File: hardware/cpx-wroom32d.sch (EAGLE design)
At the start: 39 parts, among them Q1 mmbt2222, Q2 mmbt2222, U1 ESP32-WROOM-32D

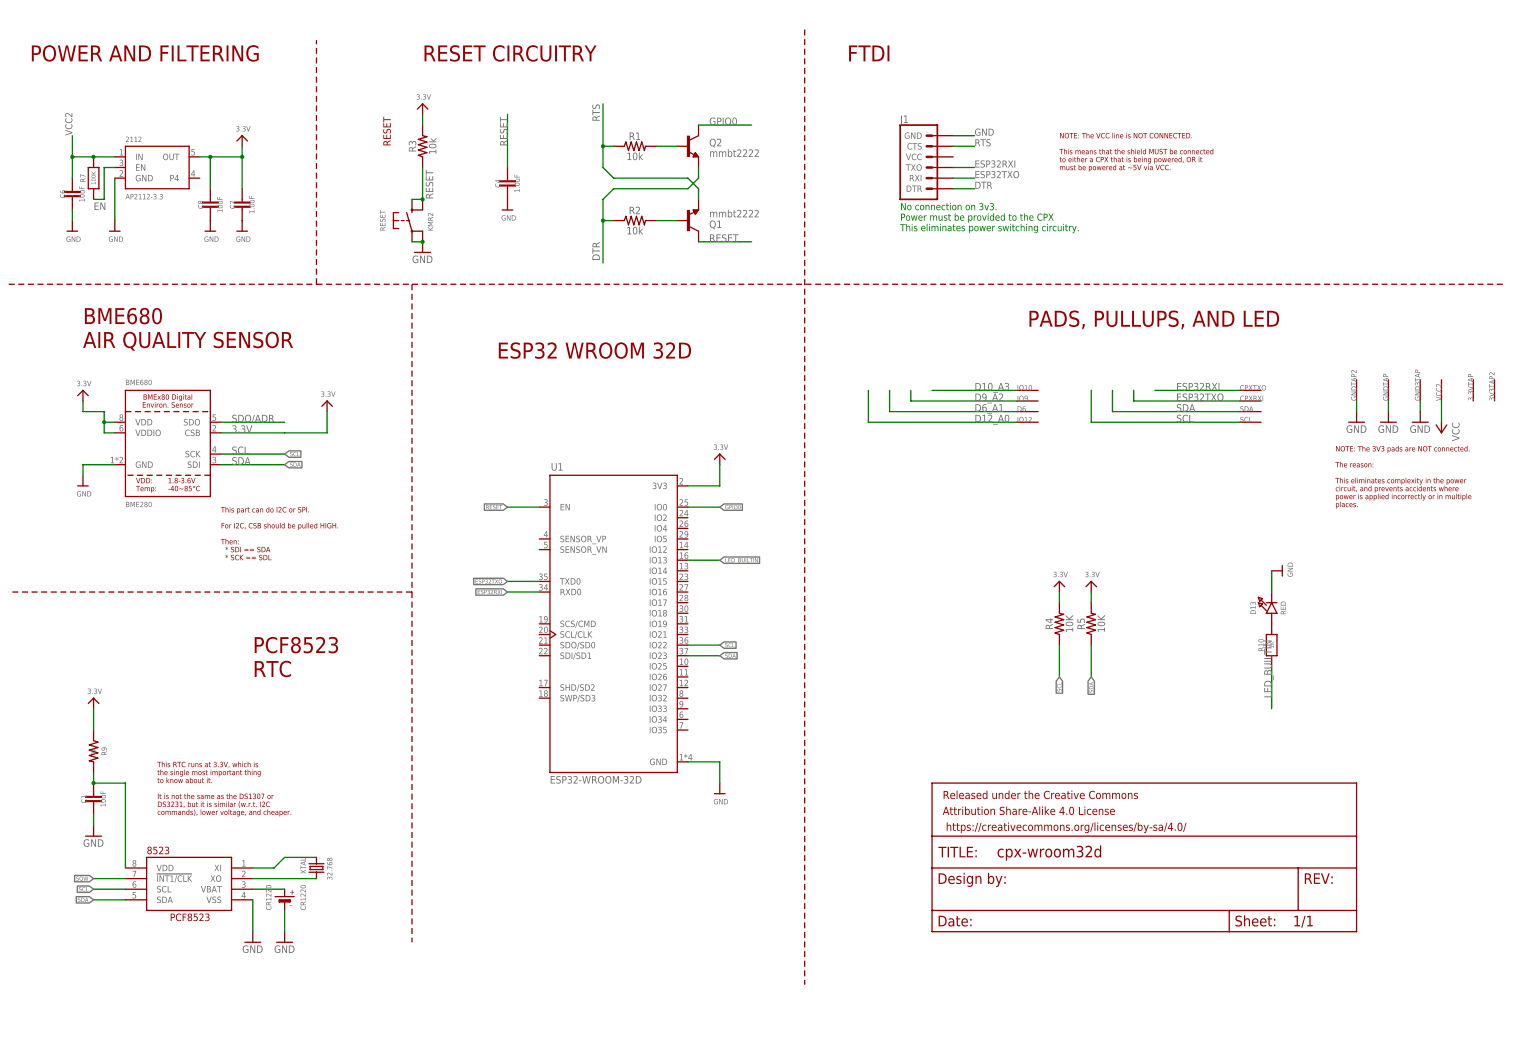
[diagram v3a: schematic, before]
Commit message: Cleaned up labeling, schematic.
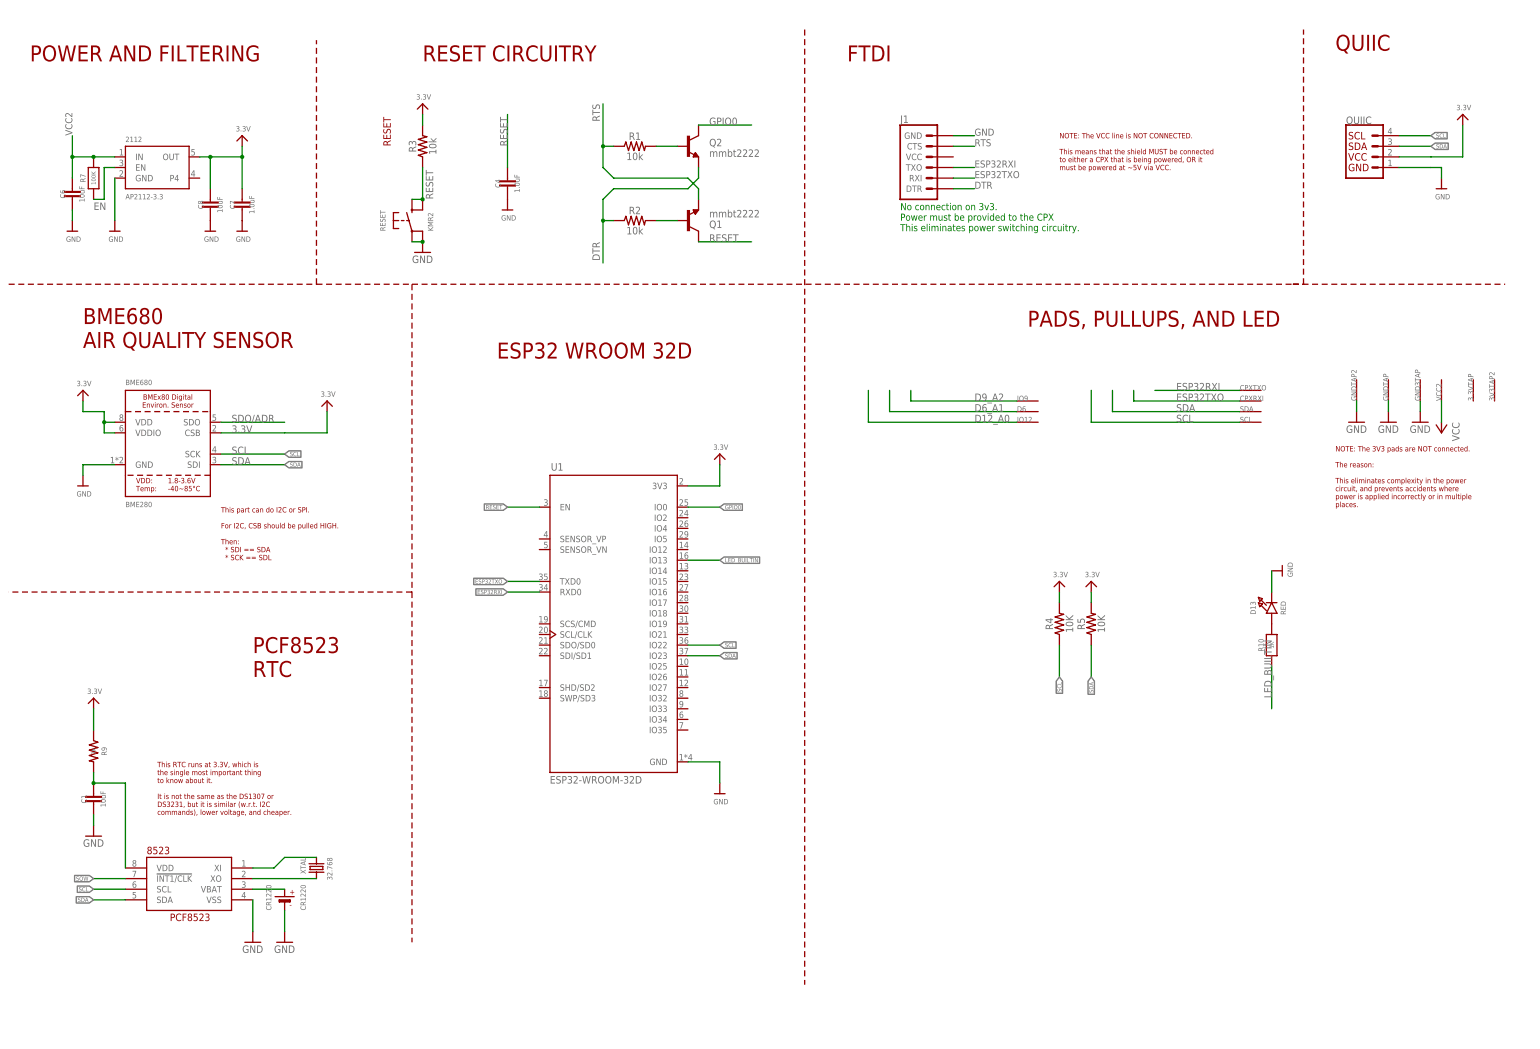
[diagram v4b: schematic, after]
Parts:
- removed FRAME1: FRAME-LETTERNO_PACKAGE, SparkFun-Aesthetics:FRAME-LETTERNO_PACKAGE
- removed IO10: SEWTAP-ALLIGATOR, microbuilder:SEWTAP-ALLIGATOR
- added QUIIC: (no value), SparkFun-Connectors:QWIIC_CONNECTORJS-1MM
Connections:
- removed net D10_A3: IO10.SEW
- net 3.3V: now also QUIIC.VCC
- net GND: now also QUIIC.GND
- net SCL: now also QUIIC.SCL
- net SDA: now also QUIIC.SDA
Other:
- note added: "QUIIC"
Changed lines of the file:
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@@
 <part name="SDA" library="microbuilder" deviceset="SEWTAP" device="-ALLIGATOR"/>
 <part name="P+2" library="supply1" deviceset="VCC" device=""/>
-<part name="IO10" library="microbuilder" deviceset="SEWTAP" device="-ALLIGATOR"/>
 <part name="IO9" library="microbuilder" deviceset="SEWTAP" device="-ALLIGATOR"/>
 <part name="D6" library="microbuilder" deviceset="SEWTAP" device="-ALLIGATOR"/>
@@
 <part name="U$12" library="microbuilder" deviceset="3.3V" device=""/>
 <part name="U$9" library="microbuilder" deviceset="3.3V" device=""/>
-<part name="FRAME1" library="SparkFun-Aesthetics" library_urn="urn:adsk.eagle:library:507" deviceset="FRAME-LETTER" device="NO_PACKAGE" package3d_urn="urn:adsk.eagle:package:37104/1"/>
+<part name="QUIIC" library="SparkFun-Connectors" library_urn="urn:adsk.eagle:library:513" deviceset="QWIIC_CONNECTOR" device="JS-1MM" package3d_urn="urn:adsk.eagle:package:38096/1"/>
+<part name="U$11" library="microbuilder" deviceset="3.3V" device=""/>
+<part name="U$14" library="microbuilder" deviceset="GND" device=""/>
 </parts>
 <sheets>
@@
 <wire x1="12.7" y1="187.96" x2="86.36" y2="187.96" width="0.1524" layer="94" style="shortdash"/>
 <wire x1="86.36" y1="187.96" x2="109.22" y2="187.96" width="0.1524" layer="94" style="shortdash"/>
-<wire x1="109.22" y1="187.96" x2="370.84" y2="187.96" width="0.1524" layer="94" style="shortdash"/>
+<wire x1="109.22" y1="187.96" x2="320.04" y2="187.96" width="0.1524" layer="94" style="shortdash"/>
+<wire x1="320.04" y1="187.96" x2="370.84" y2="187.96" width="0.1524" layer="94" style="shortdash"/>
 <wire x1="203.2" y1="248.92" x2="203.2" y2="20.32" width="0.1524" layer="94" style="shortdash"/>
 <wire x1="109.22" y1="187.96" x2="109.22" y2="114.3" width="0.1524" layer="94" style="shortdash"/>
@@
 power is applied incorrectly or in multiple
 places.</text>
+<wire x1="320.04" y1="187.96" x2="322.58" y2="187.96" width="0.1524" layer="94" style="shortdash"/>
+<wire x1="322.58" y1="187.96" x2="322.58" y2="248.92" width="0.1524" layer="94" style="shortdash"/>
+<text x="330.2" y="243.84" size="3.81" layer="94" font="vector" ratio="12">QUIIC</text>
 </plain>
 <instances>
@@
 <attribute name="VALUE" x="358.14" y="154.94" size="1.778" layer="96" rot="R270"/>
 </instance>
-<instance part="IO10" gate="G$1" x="254" y="162.56" smashed="yes">
-<attribute name="NAME" x="254" y="162.56" size="1.27" layer="95" font="vector"/>
-</instance>
 <instance part="IO9" gate="G$1" x="254" y="160.02" smashed="yes">
 <attribute name="NAME" x="254" y="160.02" size="1.27" layer="95" font="vector"/>
@@
 <attribute name="VALUE" x="87.376" y="161.036" size="1.27" layer="96"/>
 </instance>
-<instance part="FRAME1" gate="V" x="233.68" y="33.02" smashed="yes">
-<attribute name="LAST_DATE_TIME" x="246.38" y="34.29" size="2.54" layer="94" font="vector"/>
-<attribute name="SHEET" x="320.04" y="34.29" size="2.54" layer="94" font="vector"/>
-<attribute name="DRAWING_NAME" x="249.174" y="50.8" size="2.7432" layer="94" font="vector"/>
+<instance part="QUIIC" gate="J1" x="337.82" y="218.44" smashed="yes">
+<attribute name="VALUE" x="332.74" y="213.106" size="1.778" layer="96" font="vector" align="top-left"/>
+<attribute name="NAME" x="332.74" y="226.314" size="1.778" layer="95" font="vector"/>
+</instance>
+<instance part="U$11" gate="G$1" x="360.68" y="228.6" smashed="yes">
+<attribute name="VALUE" x="359.156" y="229.616" size="1.27" layer="96"/>
+</instance>
+<instance part="U$14" gate="G$1" x="355.6" y="210.82" smashed="yes">
+<attribute name="VALUE" x="354.076" y="208.28" size="1.27" layer="96"/>
 </instance>
 </instances>
@@
 <pinref part="U$4" gate="G$1" pin="GND"/>
 <pinref part="BME680" gate="G$1" pin="GND"/>
+</segment>
+<segment>
+<pinref part="QUIIC" gate="J1" pin="GND"/>
+<wire x1="345.44" y1="215.9" x2="353.06" y2="215.9" width="0.1524" layer="91"/>
+<pinref part="U$14" gate="G$1" pin="GND"/>
+<wire x1="353.06" y1="215.9" x2="355.6" y2="215.9" width="0.1524" layer="91"/>
+<wire x1="355.6" y1="215.9" x2="355.6" y2="213.36" width="0.1524" layer="91"/>
 </segment>
 </net>
@@
 <pinref part="U$9" gate="G$1" pin="3.3V"/>
 </segment>
+<segment>
+<pinref part="QUIIC" gate="J1" pin="VCC"/>
+<wire x1="345.44" y1="218.44" x2="353.06" y2="218.44" width="0.1524" layer="91"/>
+<wire x1="353.06" y1="218.44" x2="360.68" y2="218.44" width="0.1524" layer="91"/>
+<wire x1="360.68" y1="218.44" x2="360.68" y2="226.06" width="0.1524" layer="91"/>
+<pinref part="U$11" gate="G$1" pin="3.3V"/>
+</segment>
 </net>
 <net name="D12_A0" class="0">
@@
 <label x="78.74" y="147.32" size="1.016" layer="95" xref="yes"/>
 </segment>
+<segment>
+<pinref part="QUIIC" gate="J1" pin="SCL"/>
+<wire x1="345.44" y1="223.52" x2="353.06" y2="223.52" width="0.1524" layer="91"/>
+<label x="353.06" y="223.52" size="1.016" layer="95" xref="yes"/>
+</segment>
 </net>
 <net name="SDA" class="0">
@@
 <label x="78.74" y="144.78" size="1.016" layer="95" xref="yes"/>
 </segment>
+<segment>
+<pinref part="QUIIC" gate="J1" pin="SDA"/>
+<wire x1="345.44" y1="220.98" x2="353.06" y2="220.98" width="0.1524" layer="91"/>
+<label x="353.06" y="220.98" size="1.016" layer="95" xref="yes"/>
+</segment>
 </net>
 <net name="ESP32TXO" class="0">
@@
 </segment>
 </net>
-<net name="D10_A3" class="0">
-<segment>
-<wire x1="233.68" y1="162.56" x2="254" y2="162.56" width="0.1524" layer="91"/>
-<label x="243.84" y="162.56" size="1.778" layer="95"/>
-<pinref part="IO10" gate="G$1" pin="SEW"/>
-</segment>
-</net>

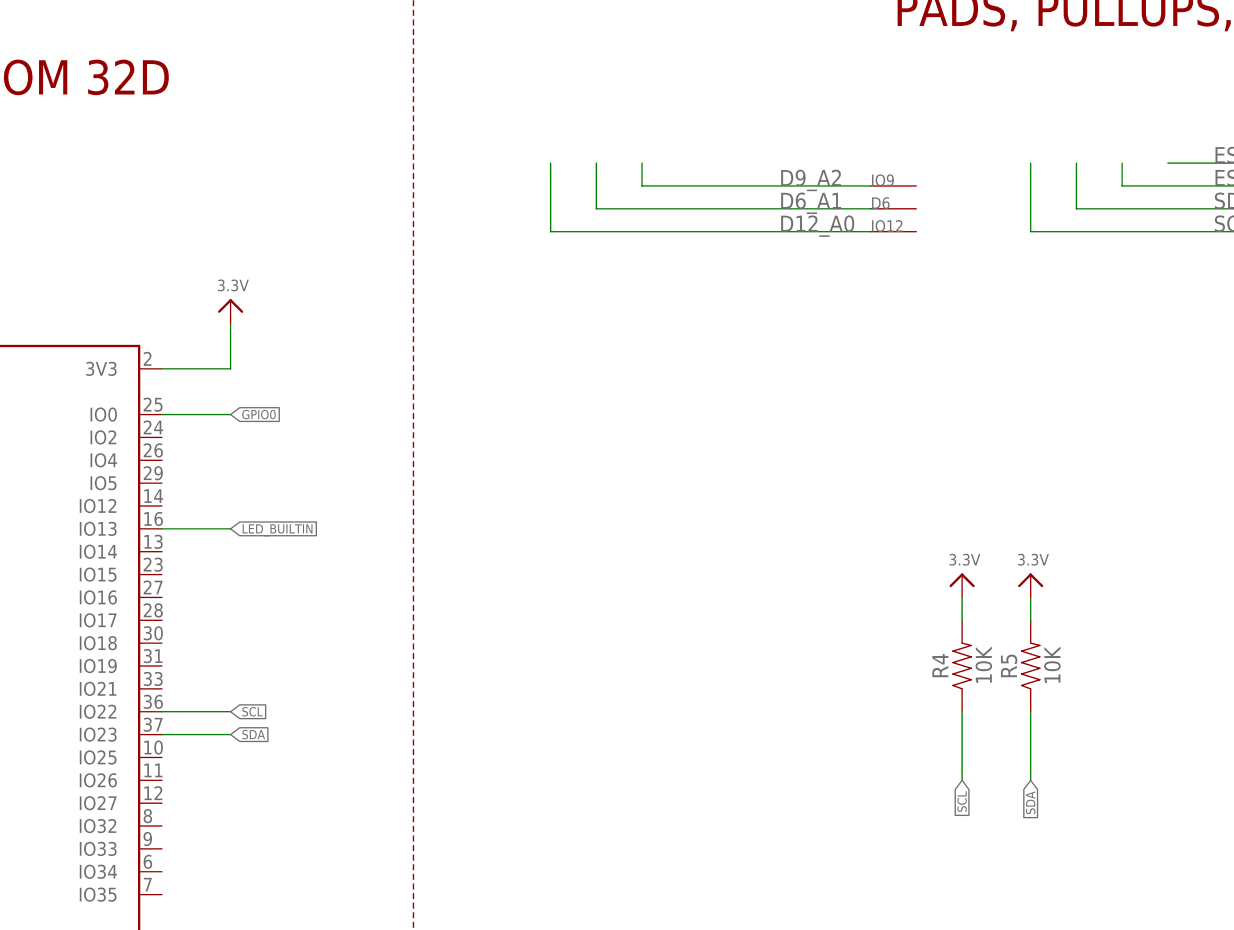
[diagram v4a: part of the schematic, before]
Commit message: Forgot .gitignore, updates.
* Added a wakeup line to A2 on the CPX.
  Toggling this is to trigger the external interrupt on
  the ESP32. This seems better than playing games with RX/TX

* Moved BME680 a bit, to get it away from the QUIIC connector.

* Exploring sleep. Need to think about what I want for a serial protocol. Line-oriented? Byte-oriented?

I'd rather we were using I2C for this, but for the team, we're using Python.
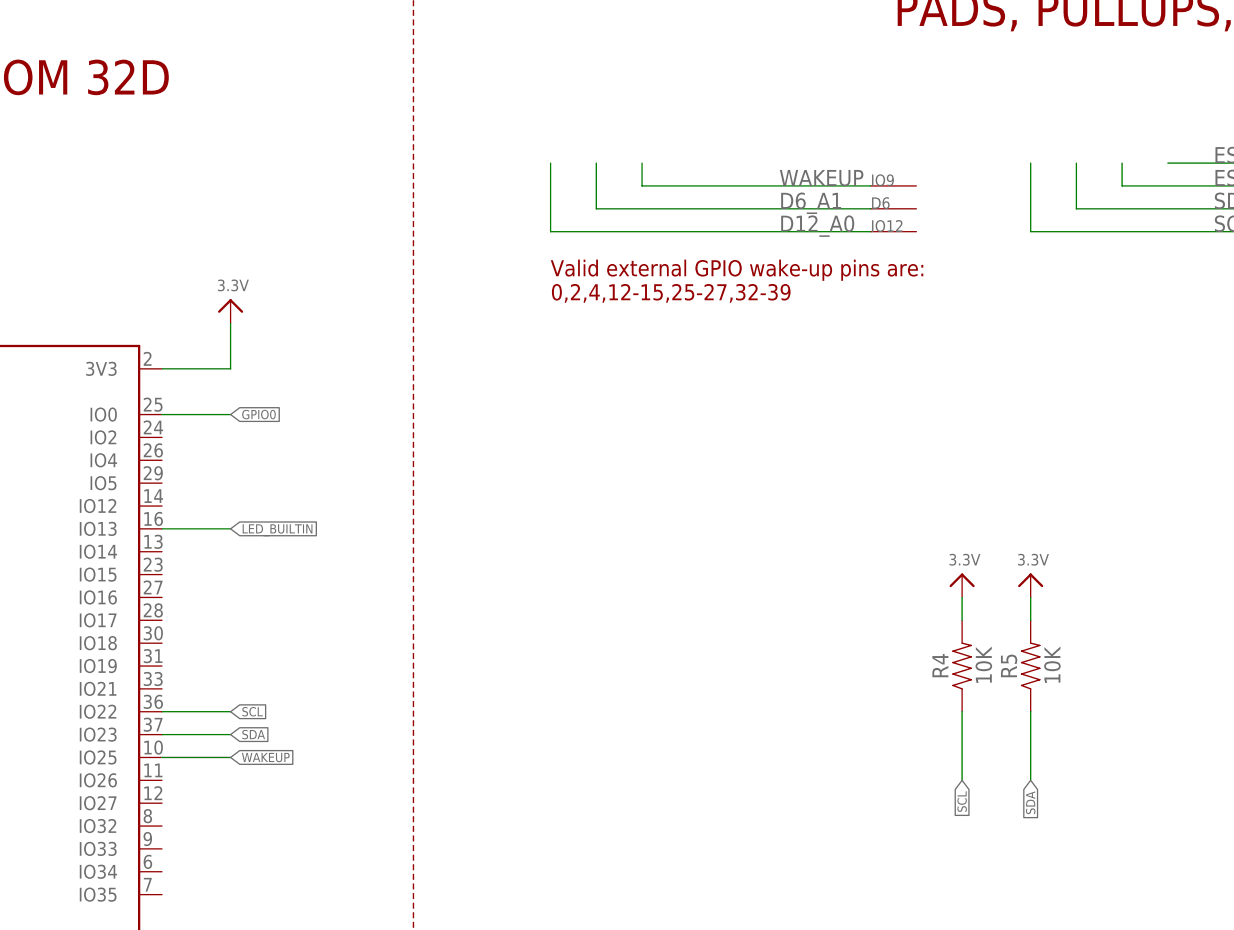
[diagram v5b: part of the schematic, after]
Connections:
- removed net D9_A2: IO9.SEW
- new net WAKEUP: IO9.SEW, U1.IO25
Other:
- note added: "Valid external GPIO wake-up pins are: 0,2,4,12-15,25-27,32-39"
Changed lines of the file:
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@@
 <wire x1="322.58" y1="187.96" x2="322.58" y2="248.92" width="0.1524" layer="94" style="shortdash"/>
 <text x="330.2" y="243.84" size="3.81" layer="94" font="vector" ratio="12">QUIIC</text>
+<text x="218.44" y="147.32" size="1.778" layer="94" font="vector">Valid external GPIO wake-up pins are:
+0,2,4,12-15,25-27,32-39</text>
 </plain>
 <instances>
@@
 </segment>
 </net>
-<net name="D9_A2" class="0">
-<segment>
-<wire x1="228.6" y1="160.02" x2="254" y2="160.02" width="0.1524" layer="91"/>
-<label x="243.84" y="160.02" size="1.778" layer="95"/>
-<pinref part="IO9" gate="G$1" pin="SEW"/>
-<wire x1="228.6" y1="160.02" x2="228.6" y2="162.56" width="0.1524" layer="91"/>
-</segment>
-</net>
 <net name="RESET" class="0">
 <segment>
@@
 </segment>
 </net>
+<net name="WAKEUP" class="0">
+<segment>
+<pinref part="U1" gate="G$1" pin="IO25"/>
+<wire x1="175.26" y1="96.52" x2="182.88" y2="96.52" width="0.1524" layer="91"/>
+<label x="182.88" y="96.52" size="1.016" layer="95" xref="yes"/>
+</segment>
+<segment>
+<wire x1="228.6" y1="160.02" x2="254" y2="160.02" width="0.1524" layer="91"/>
+<label x="243.84" y="160.02" size="1.778" layer="95"/>
+<pinref part="IO9" gate="G$1" pin="SEW"/>
+<wire x1="228.6" y1="160.02" x2="228.6" y2="162.56" width="0.1524" layer="91"/>
+</segment>
+</net>
